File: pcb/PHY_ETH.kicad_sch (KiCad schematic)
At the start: 32 parts, among them U3 LAN8742A, Y1 LFXTAL071758Cutt

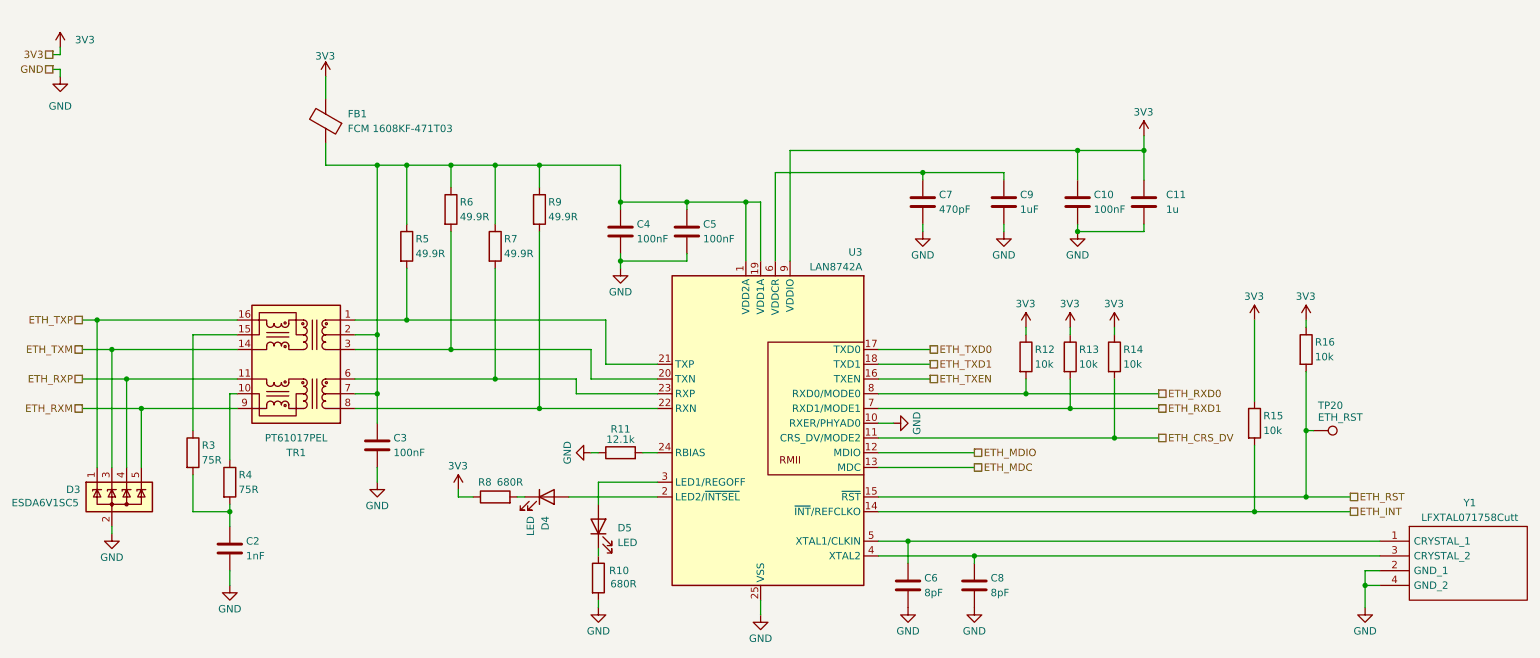
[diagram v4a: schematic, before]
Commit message: added jumper for VCAP connection to 1V2MCU. Fixed resistors on ethernet IF
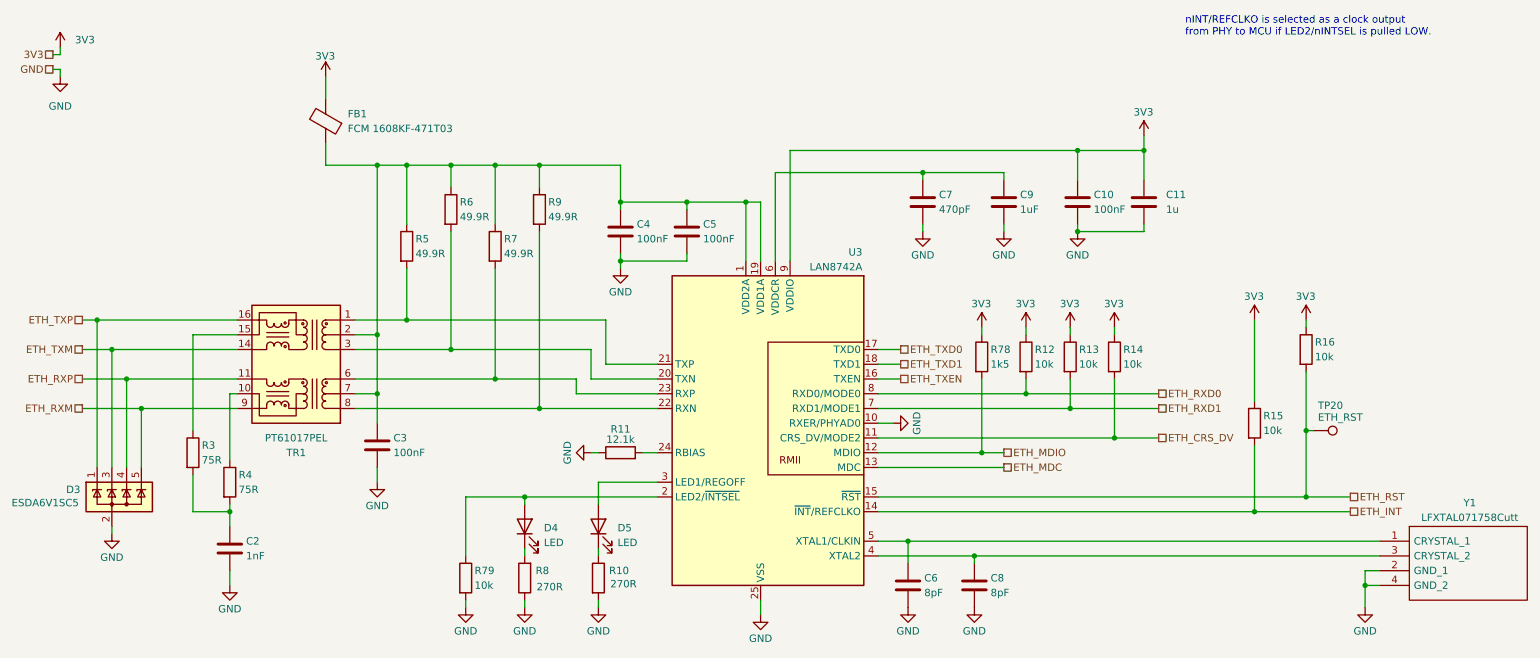
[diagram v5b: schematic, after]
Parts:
- added R78: 1k5, Resistor_SMD:R_0603_1608Metric_Pad0.98x0.95mm_HandSolder, symbol Device:R
- added R79: 10k, Resistor_SMD:R_0603_1608Metric_Pad0.98x0.95mm_HandSolder, symbol Device:R
- R10, R8: value 680R -> 270R
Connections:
- net 3V3: now also R78.1; no longer R8.1
- net ETH_MDIO: now also R78.2
- net GND: now also R8.1, R79.2
- net at D4.2 (A), U3.2 (LED2/~{INTSEL}): now also R79.1
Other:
- note added: "nINT/REFCLKO is selected as a clock output from PHY to MCU if LED2/nINTSEL is pulled LOW."
- moved on the sheet: D4, R8

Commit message: updates from bom release
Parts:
- C10, C3, C4, C5: value 100nF -> 100n
- C2: value 1nF -> 1n
- C6, C8: value 8pF -> 8p
- C7: value 470pF -> 470p
- C9: value 1uF -> 1u
- R10, R8: value 270R -> 270
- R3, R4: value 75R -> 75
- R5, R6, R7, R9: value 49.9R -> 49.9
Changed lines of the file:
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@@
 			)
 		)
-		(property "Value" "270R"
+		(property "Value" "270"
 			(at 110.998 117.094 0)
 			(effects
@@
 			)
 		)
-		(property "Value" "270R"
+		(property "Value" "270"
 			(at 123.698 116.586 0)
 			(effects
@@
 			)
 		)
-		(property "Value" "100nF"
+		(property "Value" "100n"
 			(at 204.724 52.07 0)
 			(effects
@@
 			)
 		)
-		(property "Value" "100nF"
+		(property "Value" "100n"
 			(at 84.074 93.98 0)
 			(effects
@@
 			)
 		)
-		(property "Value" "1nF"
+		(property "Value" "1n"
 			(at 58.674 111.76 0)
 			(effects
@@
 			)
 		)
-		(property "Value" "100nF"
+		(property "Value" "100n"
 			(at 125.984 57.15 0)
 			(effects
@@
 			)
 		)
-		(property "Value" "8pF"
+		(property "Value" "8p"
 			(at 186.944 118.11 0)
 			(effects
@@
 			)
 		)
-		(property "Value" "49.9R"
+		(property "Value" "49.9"
 			(at 110.744 53.34 0)
 			(effects
@@
 			)
 		)
-		(property "Value" "100nF"
+		(property "Value" "100n"
 			(at 137.414 57.15 0)
 			(effects
@@
 			)
 		)
-		(property "Value" "75R"
+		(property "Value" "75"
 			(at 51.054 95.25 0)
 			(effects
@@
 			)
 		)
-		(property "Value" "75R"
+		(property "Value" "75"
 			(at 57.404 100.33 0)
 			(effects
@@
 			)
 		)
-		(property "Value" "470pF"
+		(property "Value" "470p"
 			(at 178.054 52.07 0)
 			(effects
@@
 			)
 		)
-		(property "Value" "1uF"
+		(property "Value" "1u"
 			(at 192.024 52.07 0)
 			(effects
@@
 			)
 		)
-		(property "Value" "49.9R"
+		(property "Value" "49.9"
 			(at 103.124 59.69 0)
 			(effects
@@
 			)
 		)
-		(property "Value" "8pF"
+		(property "Value" "8p"
 			(at 175.514 118.11 0)
 			(effects
@@
 			)
 		)
-		(property "Value" "49.9R"
+		(property "Value" "49.9"
 			(at 87.884 59.69 0)
 			(effects
@@
 			)
 		)
-		(property "Value" "49.9R"
+		(property "Value" "49.9"
 			(at 95.504 53.34 0)
 			(effects
